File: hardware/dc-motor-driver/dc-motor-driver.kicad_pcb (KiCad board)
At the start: 2 copper layers, 100 x 90 mm, 79 parts, among them J1 VIN, J10 MOT, J12 MOT, J14 MOT, J3 DE9, J4 MOT, J6 MOT, J8 MOT, U1 DRV8874PWPR, U2 DRV8874PWPR, U3 DRV8874PWPR, U4 DRV8874PWPR, U5 DRV8874PWPR, U6 DRV8874PWPR

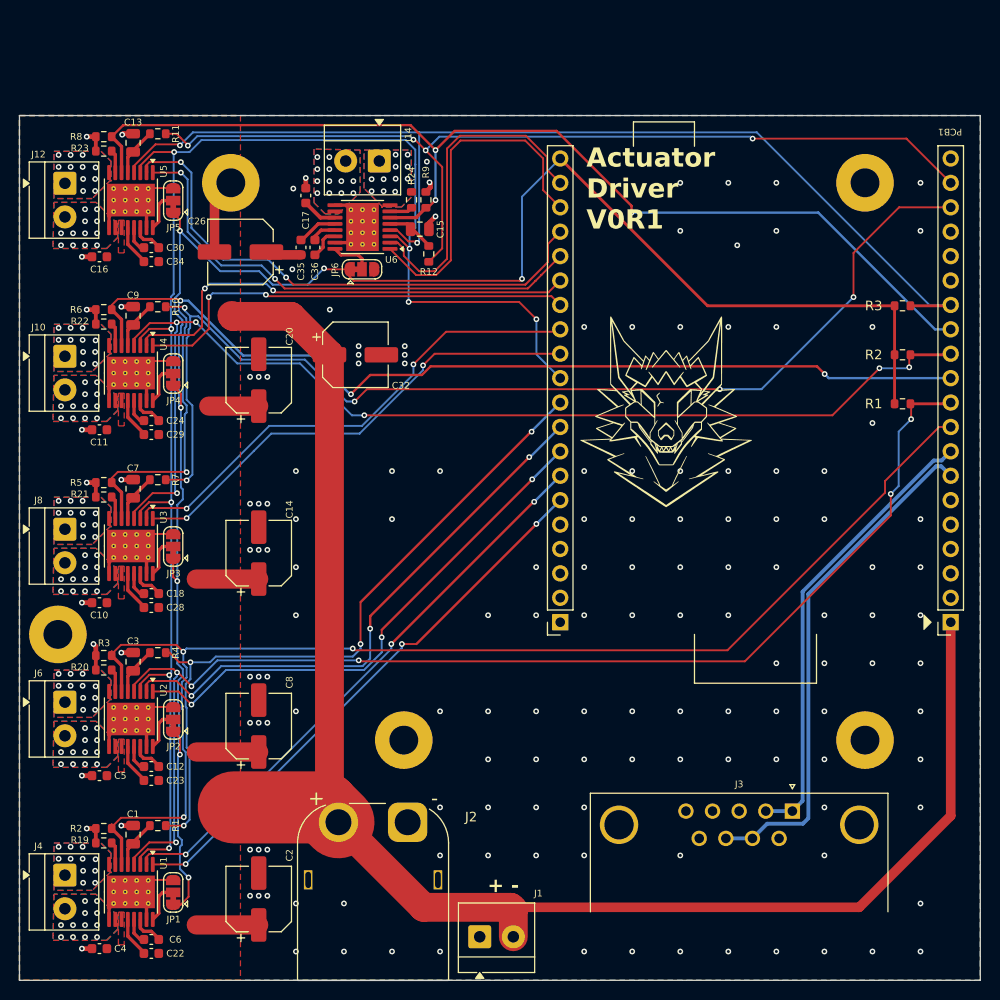
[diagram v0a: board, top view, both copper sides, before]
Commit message: Feat: Finished PCB for review
Fixed RS485 connectors, finished traces and PCB layout. Ready for review before manufacturing
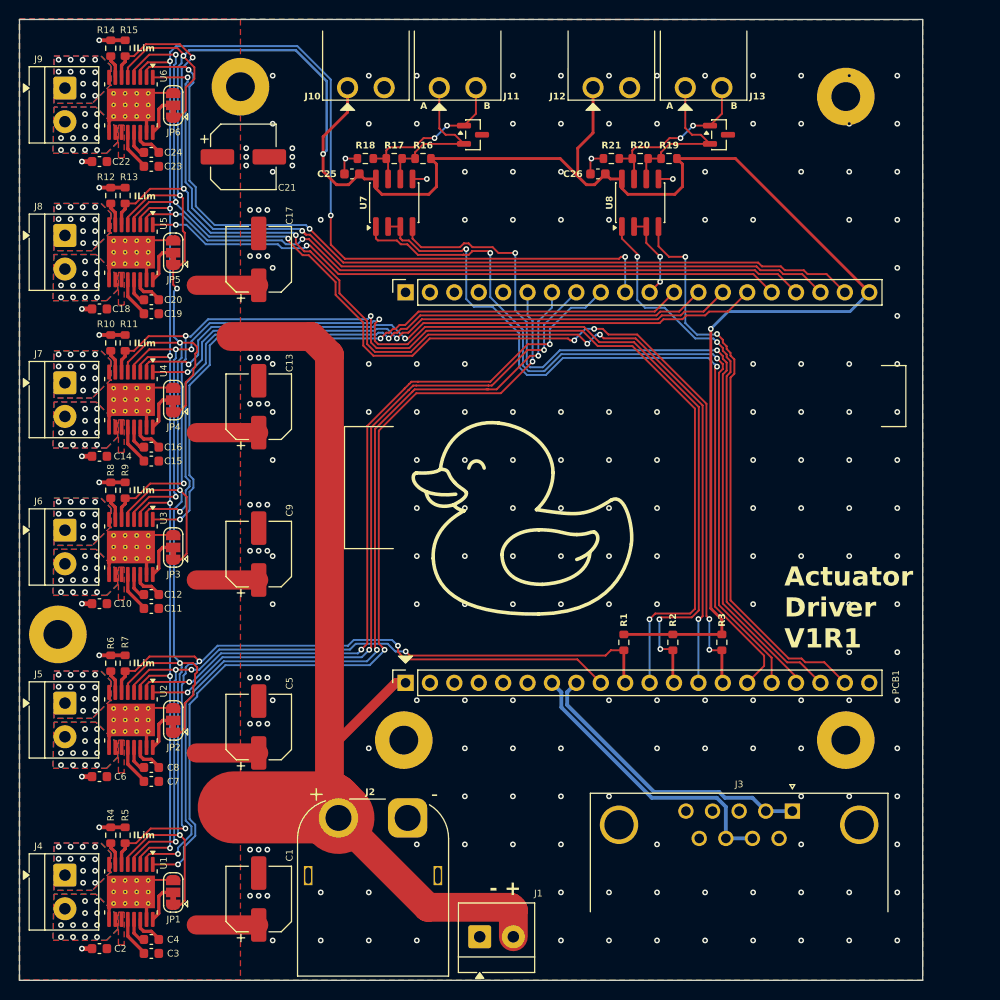
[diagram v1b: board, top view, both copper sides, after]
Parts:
- removed the C1 at (111.8, 124.8)
- removed C28, C29, C34, C35: 100n, Capacitor_SMD:C_0603_1608Metric
- removed the C3 at (111.8, 106.8)
- removed C30, C36: 22n, Capacitor_SMD:C_0603_1608Metric
- removed C32: 100u, Capacitor_SMD:CP_Elec_6.3x7.7
- removed G***: LOGO, LOGO
- removed J14: MOT, TerminalBlock_4Ucon:TerminalBlock_4Ucon_1x02_P3.50mm_Horizontal
- removed the R1 at (114.4, 123.9)
- removed the R2 at (108.8, 124.2)
- removed R22, R23, R24: 20k, Resistor_SMD:R_0603_1608Metric
- removed the R3 at (108.8, 106.2)
- added C19: 100n, Capacitor_SMD:C_0603_1608Metric, F.Cu at (113.7, 70.6)
- added C21: 100u, Capacitor_SMD:CP_Elec_6.3x7.7, F.Cu at (123.3, 54.3)
- added C22: 100n, Capacitor_SMD:C_0603_1608Metric, F.Cu at (108.3, 54.8)
- added C25: 100n, Capacitor_SMD:C_0603_1608Metric, F.Cu at (134.6, 56.1)
- added C6: 100n, Capacitor_SMD:C_0603_1608Metric, F.Cu at (108.3, 118.8)
- added D1: SM712_SOT23, Package_TO_SOT_SMD:SOT-23, F.Cu at (147.2, 52.0)
- added D2: SM712_SOT23, Package_TO_SOT_SMD:SOT-23, F.Cu at (172.8, 52.0)
- added J11: OQ0232510000G, ConnectorsOther:AnyTek_OQ_3.81mm_90_2P_TriangleKeyLock, F.Cu at (145.6, 43.7)
- added J13: OQ0232510000G, ConnectorsOther:AnyTek_OQ_3.81mm_90_2P_TriangleKeyLock, F.Cu at (171.2, 43.7)
- added J5: MOT, TerminalBlock_4Ucon:TerminalBlock_4Ucon_1x02_P3.50mm_Horizontal, F.Cu at (104.7, 111.2)
- added J7: MOT, TerminalBlock_4Ucon:TerminalBlock_4Ucon_1x02_P3.50mm_Horizontal, F.Cu at (104.7, 77.8)
- added J9: MOT, TerminalBlock_4Ucon:TerminalBlock_4Ucon_1x02_P3.50mm_Horizontal, F.Cu at (104.7, 47.1)
- added R13: 1k3, Resistor_SMD:R_0603_1608Metric, F.Cu at (111.0, 58.3)
- added R14: 20k, Resistor_SMD:R_0603_1608Metric, F.Cu at (109.5, 43.0)
- added R15: 1k3, Resistor_SMD:R_0603_1608Metric, F.Cu at (111.0, 43.0)
- added R16: 330, Resistor_SMD:R_0603_1608Metric, F.Cu at (142.0, 54.5)
- added R17: 120, Resistor_SMD:R_0603_1608Metric, F.Cu at (139.0, 54.5)
- added R18: 330, Resistor_SMD:R_0603_1608Metric, F.Cu at (136.0, 54.5)
- added U7: SP3485CN, Package_SO:SOIC-8_3.9x4.9mm_P1.27mm, F.Cu at (139.0, 59.1)
- added U8: SP3485CN, Package_SO:SOIC-8_3.9x4.9mm_P1.27mm, F.Cu at (164.6, 59.1)
- C13, C9: value 10u -> 100u; footprint Capacitor_SMD:C_0805_2012Metric -> Capacitor_SMD:CP_Elec_6.3x7.7
- C14, C26: value 100u -> 100n; footprint Capacitor_SMD:CP_Elec_6.3x7.7 -> Capacitor_SMD:C_0603_1608Metric
- C15, C7: value 10u -> 100n; footprint Capacitor_SMD:C_0805_2012Metric -> Capacitor_SMD:C_0603_1608Metric
- C16: value 100n -> 22n
- C17, C5: value 100n -> 100u; footprint Capacitor_SMD:C_0603_1608Metric -> Capacitor_SMD:CP_Elec_6.3x7.7
- C18: value 22n -> 100n
- C20, C8: value 100u -> 22n; footprint Capacitor_SMD:CP_Elec_6.3x7.7 -> Capacitor_SMD:C_0603_1608Metric
- J10, J12: value MOT -> OQ0232510000G; footprint TerminalBlock_4Ucon:TerminalBlock_4Ucon_1x02_P3.50mm_Horizontal -> ConnectorsOther:AnyTek_OQ_3.81mm_90_2P_TriangleKeyLock
- R10, R12, R4: value 10k -> 20k
- R11, R7: value 10k -> 1k3
- R19, R21: value 20k -> 330
- R20: value 20k -> 120
- R5, R9: value 2k2 -> 1k3
- R6, R8: value 2k2 -> 20k
- moved R19 92.4 mm to (167.6, 54.5)
- moved R20 77.1 mm to (164.6, 54.5)
- moved C23 63.9 mm to (113.7, 55.3)
- moved R21 63.5 mm to (161.6, 54.5)
- moved J12 58.4 mm to (161.6, 43.7), turned to 0 degrees
- moved J10 44.3 mm to (136.1, 43.7), turned to 0 degrees
- moved R9 43.5 mm to (111.0, 89.0)
- moved R3 39.8 mm to (173.1, 104.8), turned to 90 degrees
- moved R2 38.3 mm to (168.0, 104.8), turned to 90 degrees
- moved R1 38.2 mm to (162.9, 104.8), turned to 90 degrees
- moved C26 38.1 mm to (160.2, 56.1)
- moved C15 36.9 mm to (113.7, 86.0), turned to 180 degrees
- moved R6 36.8 mm to (109.5, 107.0), turned to 90 degrees
- moved R8 36.8 mm to (109.5, 89.0), turned to 90 degrees
- moved R5 36.8 mm to (111.0, 124.9), turned to 90 degrees
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- renumbered C2 to C1, C4 to C2, C22 to C3, C6 to C4
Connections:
- C11 pad 2: GND -> Net-(U3-VCP)
- C12 pad 1: Net-(U2-CPH) -> Net-(U3-CPH)
- C12 pad 2: Net-(U2-CPL) -> Net-(U3-CPL)
- C13 pad 1: Net-(U5-VREF) -> VCC
- C15 pad 1: Net-(U6-VREF) -> VCC
- C15 pad 2: GND -> Net-(U4-VCP)
- C16 pad 1: VCC -> Net-(U4-CPH)
- C16 pad 2: GND -> Net-(U4-CPL)
- C18 pad 1: Net-(U3-CPH) -> VCC
- C18 pad 2: Net-(U3-CPL) -> GND
- C20 pad 1: VCC -> Net-(U5-CPH)
- C20 pad 2: GND -> Net-(U5-CPL)
- C23 pad 2: Net-(U2-VCP) -> Net-(U6-VCP)
- C24 pad 1: Net-(U4-CPH) -> Net-(U6-CPH)
- C24 pad 2: Net-(U4-CPL) -> Net-(U6-CPL)
- C26 pad 1: VCC -> +3V3
- C7 pad 1: Net-(U3-VREF) -> VCC
- C7 pad 2: GND -> Net-(U2-VCP)
- C8 pad 1: VCC -> Net-(U2-CPH)
- C8 pad 2: GND -> Net-(U2-CPL)
- C9 pad 1: Net-(U4-VREF) -> VCC
- J10 pad 1: Net-(J10-Pin_1) -> +3V3
- J10 pad 2: Net-(J10-Pin_2) -> GND
- J12 pad 1: Net-(J12-Pin_1) -> +3V3
- J12 pad 2: Net-(J12-Pin_2) -> GND
- PCB1 pad 15: unconnected-(PCB1-A7-Pad15) -> /MCU1_DIR
- PCB1 pad 16: unconnected-(PCB1-A8-Pad16) -> /MCU1_RX
- PCB1 pad 17: unconnected-(PCB1-A9-Pad17) -> /MCU1_TX
- PCB1 pad 18: unconnected-(PCB1-A10-Pad18) -> /MCU2_RX
- PCB1 pad 19: unconnected-(PCB1-IO12-Pad19) -> /MCU2_TX
- PCB1 pad 30: /~{SLEEP} -> /MCU2_DIR
- PCB1 pad 31: unconnected-(PCB1-IO40-Pad31) -> /~{SLEEP}
- R10 pad 1: /BANK2_ILIM -> Net-(U4-IMODE)
- R10 pad 2: Net-(U4-VREF) -> GND
- R11 pad 1: /BANK3_ILIM -> /BANK2_I_SENSE
- R11 pad 2: Net-(U5-VREF) -> GND
- R12 pad 1: /BANK3_ILIM -> Net-(U5-IMODE)
- R12 pad 2: Net-(U6-VREF) -> GND
- R19 pad 1: Net-(U1-IMODE) -> +3V3
- R19 pad 2: GND -> Net-(D2-A2)
- R20 pad 1: Net-(U2-IMODE) -> Net-(D2-A2)
- R20 pad 2: GND -> Net-(D2-A1)
- R21 pad 1: Net-(U3-IMODE) -> Net-(D2-A1)
- R4 pad 1: /BANK1_ILIM -> Net-(U1-IMODE)
- R4 pad 2: Net-(U2-VREF) -> GND
- R5 pad 1: /BANK2_I_SENSE -> /BANK1_I_SENSE
- R6 pad 1: /BANK2_I_SENSE -> Net-(U2-IMODE)
- R7 pad 1: /BANK2_ILIM -> /BANK1_I_SENSE
- R7 pad 2: Net-(U3-VREF) -> GND
- R8 pad 1: /BANK3_I_SENSE -> Net-(U3-IMODE)
- R9 pad 1: /BANK3_I_SENSE -> /BANK2_I_SENSE
- U1 pad 5: Net-(U1-VREF) -> +3V3
- U2 pad 10: Net-(J6-Pin_2) -> Net-(J5-Pin_2)
- U2 pad 5: Net-(U2-VREF) -> +3V3
- U2 pad 8: Net-(J6-Pin_1) -> Net-(J5-Pin_1)
- U3 pad 10: Net-(J8-Pin_2) -> Net-(J6-Pin_2)
- U3 pad 5: Net-(U3-VREF) -> +3V3
- U3 pad 8: Net-(J8-Pin_1) -> Net-(J6-Pin_1)
- U4 pad 10: Net-(J10-Pin_2) -> Net-(J7-Pin_2)
- U4 pad 5: Net-(U4-VREF) -> +3V3
- U4 pad 8: Net-(J10-Pin_1) -> Net-(J7-Pin_1)
- U5 pad 10: Net-(J12-Pin_2) -> Net-(J8-Pin_2)
- U5 pad 5: Net-(U5-VREF) -> +3V3
- U5 pad 8: Net-(J12-Pin_1) -> Net-(J8-Pin_1)
- U6 pad 5: Net-(U6-VREF) -> +3V3
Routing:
- net +3V3: track 189.0 -> 353.5 mm, vias 7 -> 9
- net /BANK2_ILIM: track 117.0 -> 0.00 mm, vias 5 -> 0
- net /BANK3_ILIM: track 98.7 -> 0.00 mm, vias 4 -> 0
- net /MCU1_RX: track 0.00 -> 85.1 mm, vias 0 -> 2
- net /MCU1_TX: track 0.00 -> 84.0 mm, vias 0 -> 2
- net /MCU1_DIR: track 0.00 -> 83.7 mm, vias 0 -> 2
- net /BANK1_ILIM: track 75.0 -> 0.00 mm, vias 4 -> 0
- net VCC: track 199.8 -> 139.2 mm
- net /MCU2_TX: track 0.00 -> 60.1 mm, vias 0 -> 2
- net /MCU2_RX: track 0.00 -> 59.5 mm, vias 0 -> 2
- net /MOT6_IN2: track 34.9 -> 91.5 mm, vias 0 -> 2
- net /MOT6_IN1: track 36.2 -> 86.6 mm, vias 0 -> 2
- net /BANK1_I_SENSE: track 133.6 -> 83.9 mm
- net /BANK1_~{FLT}: track 128.8 -> 81.7 mm, vias 6 -> 4
- net /MOT1_IN1: track 58.3 -> 92.6 mm
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- added copper zone on B.Cu, net Net-(J5-Pin_1)
- added copper zone on F.Cu, net Net-(J5-Pin_1)
- added copper zone on B.Cu, net Net-(J5-Pin_2)
- added copper zone on F.Cu, net Net-(J5-Pin_2)
- added copper zone on B.Cu, net Net-(J7-Pin_1)
- added copper zone on F.Cu, net Net-(J7-Pin_1)
- added copper zone on B.Cu, net Net-(J7-Pin_2)
- added copper zone on F.Cu, net Net-(J7-Pin_2)
- removed copper zone on B.Cu, net Net-(J10-Pin_1)
- removed copper zone on F.Cu, net Net-(J10-Pin_1)
- removed copper zone on B.Cu, net Net-(J10-Pin_2)
- removed copper zone on F.Cu, net Net-(J10-Pin_2)
- removed copper zone on B.Cu, net Net-(J12-Pin_1)
- removed copper zone on F.Cu, net Net-(J12-Pin_1)
- removed copper zone on B.Cu, net Net-(J12-Pin_2)
- removed copper zone on F.Cu, net Net-(J12-Pin_2)
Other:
- board size 100 x 90 mm -> 94 x 100 mm
- board text added: "A"
- board text added: "Actuator Driver V1R1"
- board text added: "B"
- board text added: "ILim"
- board text added: "JCN MRB ZEH"
- board text removed: "Actuator Driver V0R1"
- board text removed: "JCN MRB"

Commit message: Fix: Swapped Power in to match XT60 connector for consistency
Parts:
- moved J1 1.72 mm to (149.6, 135.5)
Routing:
- net VCC: track 139.2 -> 134.1 mm
- net GND: vias 216 -> 218

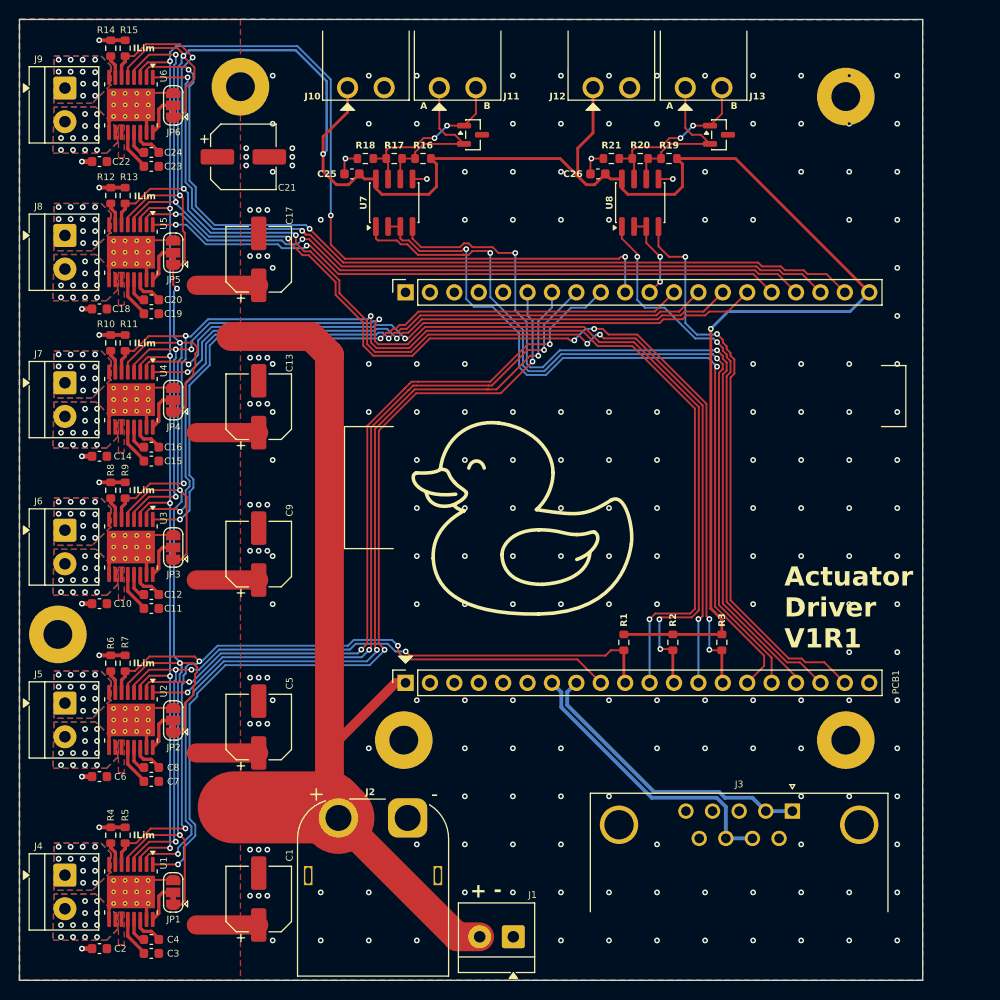
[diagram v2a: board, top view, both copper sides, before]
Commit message: Fix: PCB, schematic errors
Added M8 footprint and wiring. Fixed silkscreen issues and RS485 power out (now 24V)
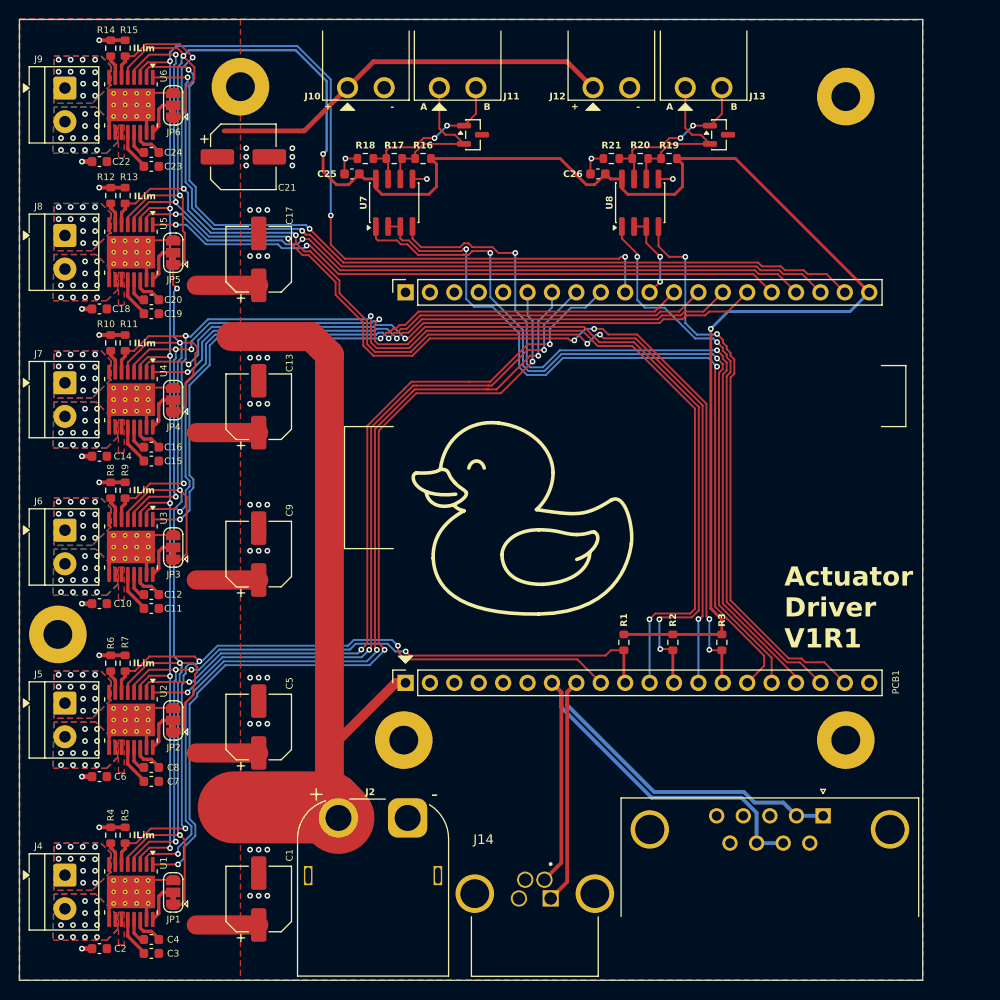
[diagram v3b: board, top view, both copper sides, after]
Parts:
- removed J1: VIN, TerminalBlock_4Ucon:TerminalBlock_4Ucon_1x02_P3.50mm_Horizontal
- added J14: 54-00274, ConnectorsOther:Tensility_M8_Socket_4P_Shielded_A, F.Cu at (153.6, 131.0)
- J2: value ~ -> VIN
- moved J3 3.24 mm to (183.6, 122.9)
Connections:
- net /CAN+ renamed /CAN_H
- net /CAN- renamed /CAN_L
- J10 pad 1: +3V3 -> VCC
- J12 pad 1: +3V3 -> VCC
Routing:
- net /CAN_L: track 30.7 -> 57.7 mm
- net /CAN_H: track 30.4 -> 55.4 mm
- net VCC: track 134.1 -> 156.8 mm
- net +3V3: track 353.5 -> 336.9 mm
- net GND: vias 218 -> 52
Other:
- board text added: "+"
- board text added: "-"
- board text removed: "- +"

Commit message: Feat: Added Via Stitching
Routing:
- net GND: vias 52 -> 212
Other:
- board text added: "ZEH MRB JCN"
- board text removed: "JCN MRB ZEH"

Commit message: added silkscreen
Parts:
- added FID1: Fiducial, Fiducial:Fiducial_1.5mm_Mask3mm, F.Cu at (191.0, 43.0)
- added FID2: Fiducial, Fiducial:Fiducial_1.5mm_Mask3mm, F.Cu at (103.0, 122.0)
- added FID3: Fiducial, Fiducial:Fiducial_1.5mm_Mask3mm, F.Cu at (191.0, 104.5)
- moved J3 6.53 mm to (183.6, 129.4)
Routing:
- net GND: vias 212 -> 211
- net /CAN_H: vias 0 -> 1
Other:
- board text added: "1"
- board text added: "2"
- board text added: "24V IN"
- board text added: "3"
- board text added: "4"
- board text added: "5"
- board text added: "6"
- board text added: "DE9 CAN"
- board text added: "M8 CAN"
- board text added: "Origin"
- board text added: "PWR"
- board text added: "RS485"
